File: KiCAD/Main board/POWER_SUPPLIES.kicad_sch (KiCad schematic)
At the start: 9 parts, among them U18 12V, U19 5V, U20 8V, U21 15V, U23 LIN_REG_±5V, U24 LIN_REG_±12V, U9 SEPIC_-15V_LT3579

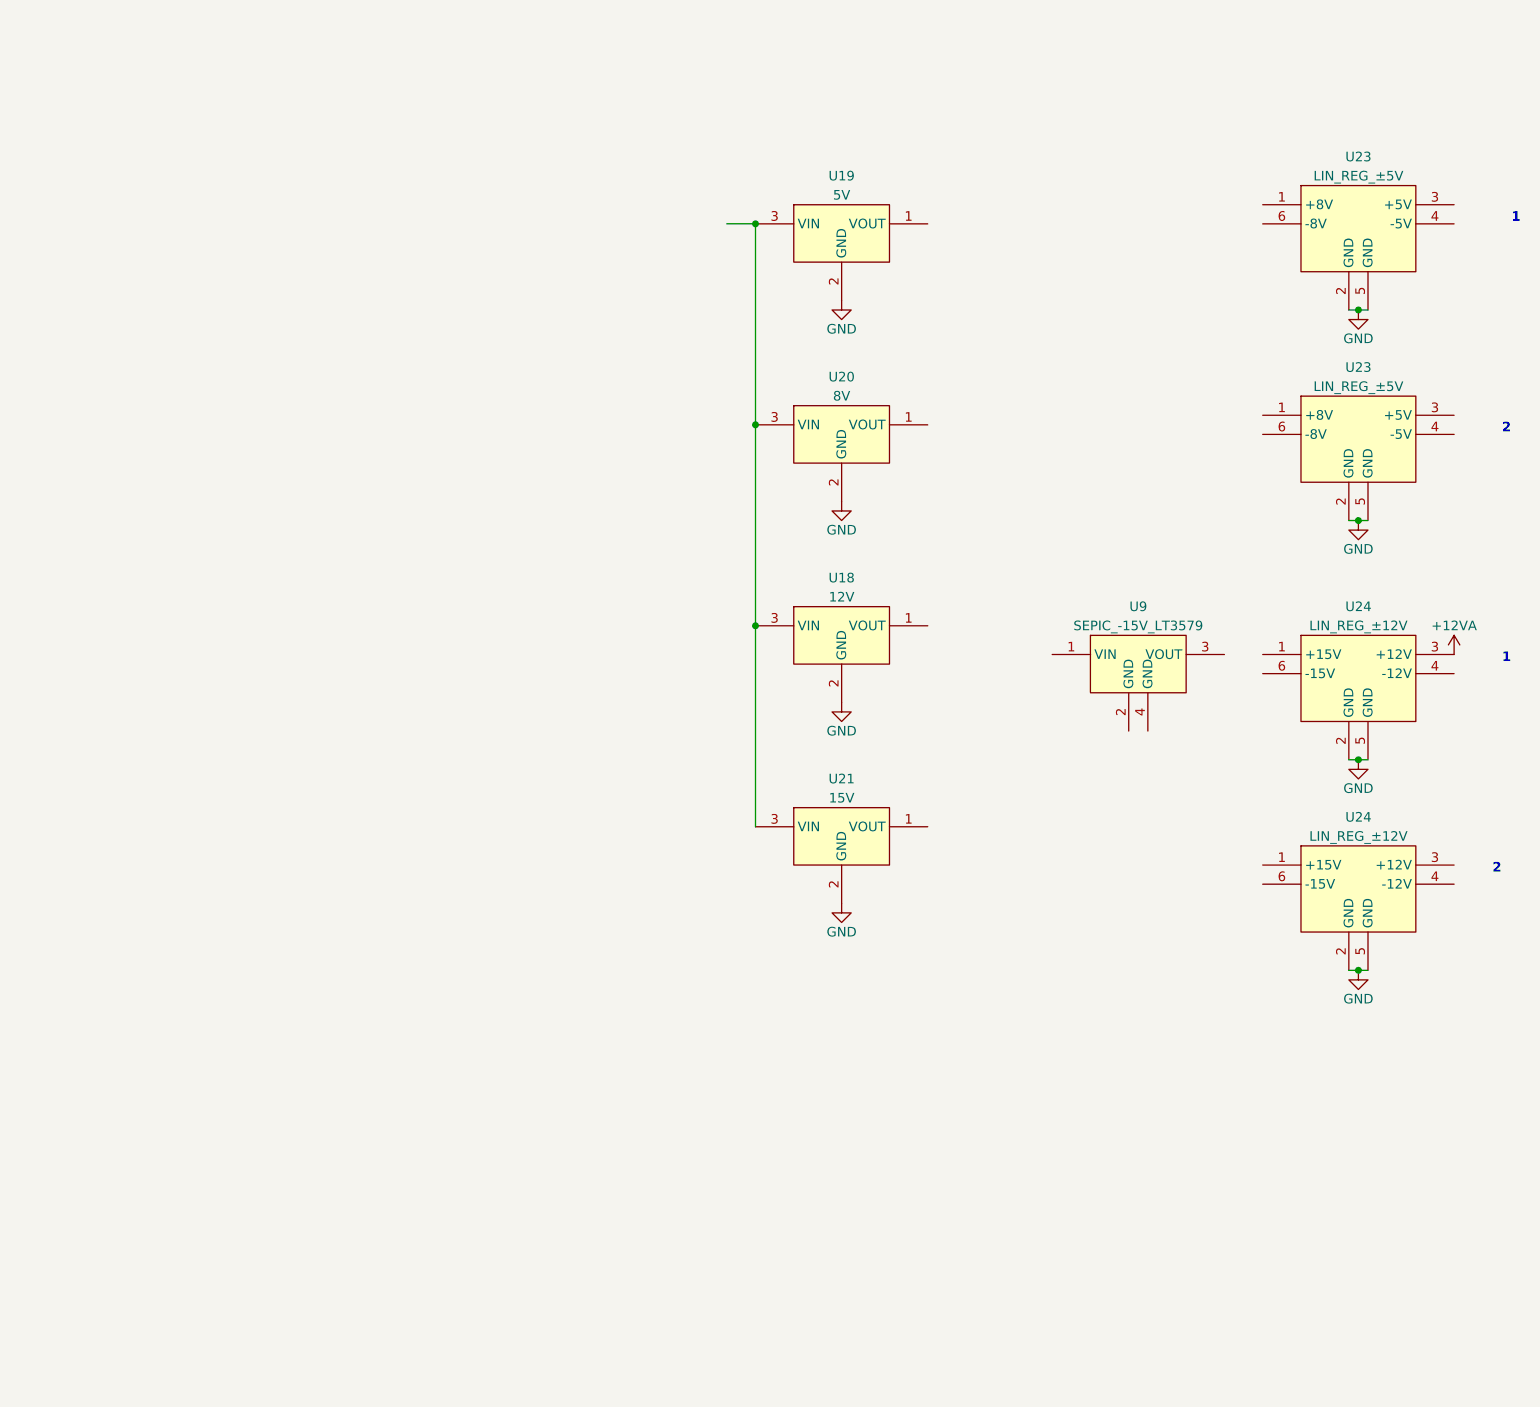
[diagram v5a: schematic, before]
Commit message: Worked on main board schematic and PCB, added symbols to symbol library
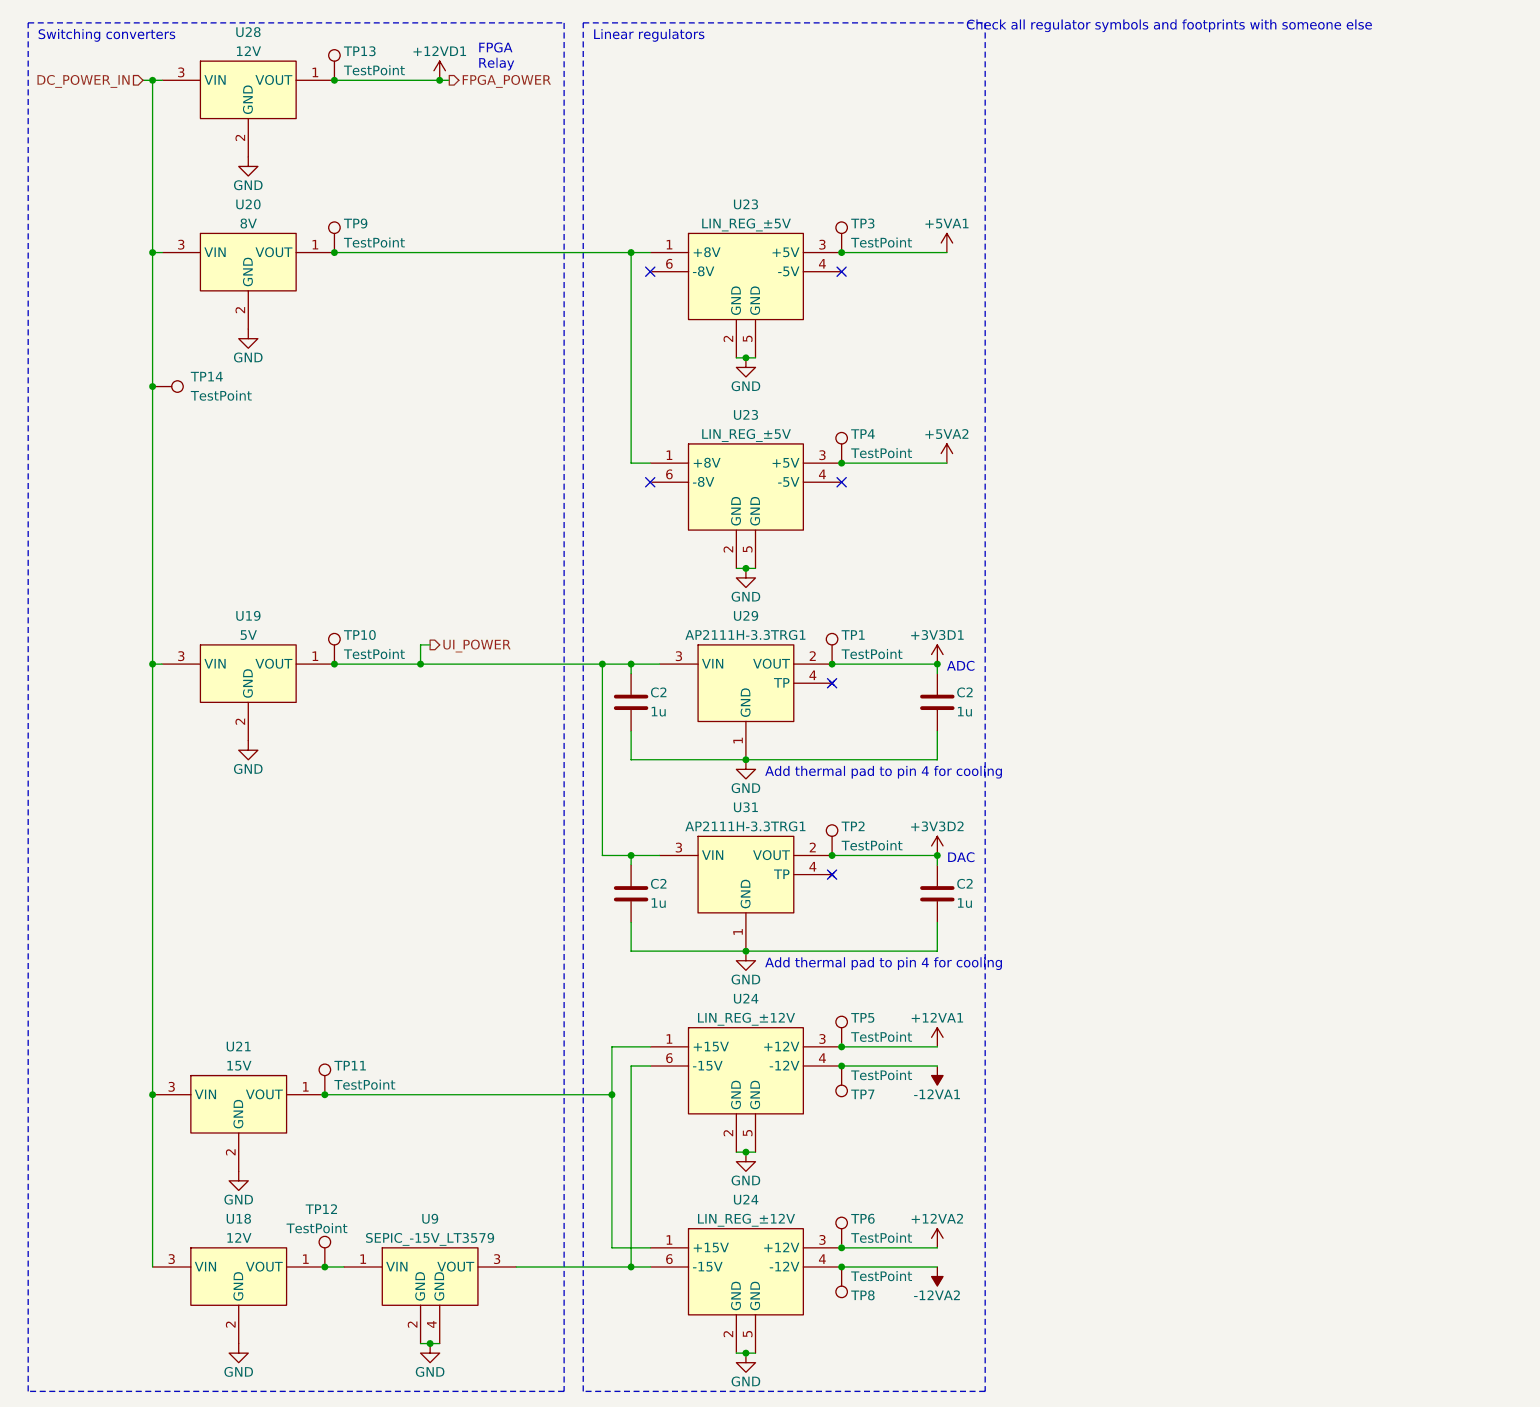
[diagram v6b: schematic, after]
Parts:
- added C2 (x4): 1u, Capacitor_SMD:C_0402_1005Metric, symbol Device:C
- added TP1, TP10, TP11, TP12, TP13, TP14, TP2, TP3, TP4, TP5, TP6, TP7, TP8, TP9: TestPoint, TestPoint:TestPoint_Pad_D2.0mm, symbol Connector:TestPoint
- added U28: 12V, Audio-DSP:BUCK_MAX17634C_xxV, symbol Audio_DSP:BUCK_12V_MAX17634C
- added U29, U31: AP2111H-3.3TRG1, Package_TO_SOT_SMD:SOT-223, symbol Audio_DSP:AP2111H-3.3TRG1
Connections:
- net GND: now also U9.2 (GND), U9.4 (GND), C2.2, C2.2, C2.2, C2.2, U28.2 (GND), U29.1 (GND), U31.1 (GND)
- net at U23.1 (+8V): now also U20.1 (VOUT), U23.1 (+8V), TP9.1
- net +5VA2: now reaches U23.3 (+5V)
- net +5VA2: now also TP4.1
- net UI_POWER: now reaches U19.1 (VOUT)
- net UI_POWER: now also C2.1, C2.1, TP10.1, U29.3 (VIN), U31.3 (VIN)
- net DC_POWER_IN: now reaches U18.3 (VIN), U19.3 (VIN), U20.3 (VIN), U21.3 (VIN)
- net DC_POWER_IN: now also TP14.1, U28.3 (VIN)
- net at U9.1 (VIN): now also U18.1 (VOUT), TP12.1
- net at U9.3 (VOUT): now also U24.6 (-15V), U24.6 (-15V)
- net at U24.1 (+15V): now also U21.1 (VOUT), U24.1 (+15V), TP11.1
- net +12VA2: now reaches U24.3 (+12V)
- net +12VA2: now also TP6.1
- net -12VA2: now reaches U24.4 (-12V)
- net -12VA2: now also TP8.1
- net +5VA1: now reaches U23.3 (+5V)
- net +5VA1: now also TP3.1
- net -12VA1: now reaches U24.4 (-12V)
- net -12VA1: now also TP7.1
- net +12VA renamed +12VA1
- net +12VA1: now also TP5.1
- new net +12VD1: TP13.1, U28.1 (VOUT)
- new net +3V3D1: C2.1, TP1.1, U29.2 (VOUT)
- new net +3V3D2: C2.1, TP2.1, U31.2 (VOUT)
- no-connect marks 0 -> 6
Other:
- note added: "ADC"
- note added: "Add thermal pad to pin 4 for cooling"
- note added: "Check all regulator symbols and footprints with someone else"
- note added: "DAC"
- note added: "FPGA Relay"
- note added: "Linear regulators"
- note added: "Switching converters"
- note removed: "1"
- note removed: "2"
- moved on the sheet: U18, U21, U23, U24, U9

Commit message: Worked on main board design
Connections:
- net UI_POWER renamed +5VD1
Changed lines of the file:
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@@
   (junction (at 67.31 189.23) (diameter 0) (color 0 0 0 0)
   )
+  (junction (at 67.31 99.06) (diameter 0) (color 0 0 0 0)
+  )
   (junction (at 93.98 179.07) (diameter 0) (color 0 0 0 0)
   )
   (junction (at 121.92 176.53) (diameter 0) (color 0 0 0 0)
   )
-  (junction (at 66.04 99.06) (diameter 0) (color 0 0 0 0)
-  )
   (junction (at 54.61 99.06) (diameter 0) (color 0 0 0 0)
   )
@@
   )
   (junction (at 30.48 62.23) (diameter 0) (color 0 0 0 0)
-  )
-  (junction (at 68.58 21.59) (diameter 0) (color 0 0 0 0)
   )
   (no_connect (at 121.92 46.99))
@@
     (stroke (width 0) (type default))
   )
-  (wire (pts (xy 66.04 96.52) (xy 66.04 99.06))
-    (stroke (width 0) (type default))
-  )
   (wire (pts (xy 109.22 111.76) (xy 134.62 111.76))
     (stroke (width 0) (type default))
@@
     (stroke (width 0) (type default))
   )
-  (wire (pts (xy 66.04 96.52) (xy 67.31 96.52))
-    (stroke (width 0) (type default))
-  )
   (wire (pts (xy 93.98 72.39) (xy 93.98 44.45))
     (stroke (width 0) (type default))
@@
     (stroke (width 0) (type default))
   )
-  (wire (pts (xy 54.61 99.06) (xy 66.04 99.06))
-    (stroke (width 0) (type default))
-  )
   (wire (pts (xy 134.62 125.73) (xy 134.62 124.46))
     (stroke (width 0) (type default))
@@
     (stroke (width 0) (type default))
   )
-  (wire (pts (xy 68.58 21.59) (xy 69.85 21.59))
-    (stroke (width 0) (type default))
-  )
   (wire (pts (xy 96.52 72.39) (xy 93.98 72.39))
     (stroke (width 0) (type default))
@@
     (stroke (width 0) (type default))
   )
-  (wire (pts (xy 66.04 99.06) (xy 90.17 99.06))
+  (wire (pts (xy 54.61 99.06) (xy 67.31 99.06))
     (stroke (width 0) (type default))
   )
@@
   )
   (wire (pts (xy 91.44 149.86) (xy 96.52 149.86))
+    (stroke (width 0) (type default))
+  )
+  (wire (pts (xy 67.31 99.06) (xy 90.17 99.06))
     (stroke (width 0) (type default))
   )
@@
     (effects (font (size 1.27 1.27)) (justify left bottom))
   )
-  (hierarchical_label "UI_POWER" (shape output) (at 67.31 96.52 0) (fields_autoplaced)
-    (effects (font (size 1.27 1.27)) (justify left))
-  )
-  (hierarchical_label "FPGA_POWER" (shape output) (at 69.85 21.59 0) (fields_autoplaced)
-    (effects (font (size 1.27 1.27)) (justify left))
-  )
   (hierarchical_label "DC_POWER_IN" (shape input) (at 29.21 21.59 180) (fields_autoplaced)
     (effects (font (size 1.27 1.27)) (justify right))
   )
+  (symbol (lib_id "Audio-DSP:+5VD1") (at 67.31 99.06 0) (unit 1)
+    (in_bom no) (on_board no) (dnp no) (fields_autoplaced)
+    (property "Reference" "#PWR0119" (at 67.31 101.6 0)
+      (effects (font (size 1.27 1.27)) hide)
+    )
+    (property "Value" "+5VD1" (at 67.31 95.25 0)
+      (effects (font (size 1.27 1.27)))
+    )
+    (property "Footprint" "" (at 67.31 99.06 0)
+      (effects (font (size 1.27 1.27)) hide)
+    )
+    (property "Datasheet" "" (at 67.31 99.06 0)
+      (effects (font (size 1.27 1.27)) hide)
+    )
+    (pin "1")
+    (instances
+      (project "Main board"
+        (path "/2f8cbac6-fd11-4240-8e40-3bb6952a0324/fc272ee1-9060-465b-85c1-b8364d68deb3"
+          (reference "#PWR0119") (unit 1)
+        )
+      )
+    )
+  )
   (symbol (lib_id "power:GND") (at 109.22 163.83 0) (unit 1)

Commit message: Worked in main board
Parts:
- removed C2 (x4): 1u, Capacitor_SMD:C_0402_1005Metric, symbol Device:C
- added C2 (x4): 1u, Capacitor_SMD:C_0402_1005Metric, symbol Device:C
- added TP15, TP16: TestPoint, TestPoint:TestPoint_Pad_D2.0mm, symbol Connector:TestPoint
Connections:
- net +3V3D1: now also TP2.1, C2.1; no longer TP1.1
- net +3V3D2: now also TP10.1, C2.1; no longer TP2.1
- net +5VD1: now also TP1.1, C2.1, C2.1; no longer TP10.1
- net GND: now also C2.2, C2.2, C2.2, C2.2
- net -5VA1: now reaches U23.4 (-5V)
- net -5VA1: now also U23.4 (-5V), TP15.1, TP16.1
- net at U23.6 (-VIN): now also U23.6 (-VIN), U24.6 (-VIN), U24.6 (-VIN), U9.3 (VOUT)
- no-connect marks 6 -> 2
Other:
- moved on the sheet: TP11, TP12, TP3, TP4, TP5, TP6, TP7, TP8, U18, U21, U23, U24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
